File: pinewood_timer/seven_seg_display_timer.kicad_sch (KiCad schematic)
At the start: 40 parts, among them M1 N-MOSFET, M10 N-MOSFET, M11 N-MOSFET, M12 N-MOSFET, M13 N-MOSFET, M14 N-MOSFET, M15 N-MOSFET, M16 N-MOSFET, M2 N-MOSFET, M3 N-MOSFET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

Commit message: did some more work on the time displays
pb and pa maybe or pc. pa might need to be adc if i cant just transistor/relay it or something
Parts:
- added R17, R18, R19, R20, R21, R22, R23, R24, R25, R26, R27, R28, R29, R30, R31, R32: 47Ω, symbol Device:R_Small_US
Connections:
- net +3.3V: now also U6.6 (E2), U7.6 (E2)
- net R3: now reaches R3.2
- net R3: now also U6.13 (~{Y2})
- net R26: now reaches R10.2
- net R26: now also U7.14 (~{Y1})
- net R31: now reaches R15.2
- net R31: now also U7.9 (~{Y6})
- net R25: now reaches R9.2
- net R25: now also U7.15 (~{Y0})
- net R28: now reaches R12.2
- net R28: now also U7.12 (~{Y3})
- net R29: now reaches R13.2
- net R29: now also U7.11 (~{Y4})
- net R6: now reaches R6.2
- net R6: now also U6.10 (~{Y5})
- net C6: now reaches U3.1
- net E: now reaches U3.11
- net E: now also U2.11, R24.2
- net D: now reaches U3.13
- net D: now also U2.13, R23.2
- net C: now reaches U3.14
- net C: now also U2.14, R22.2
- net B: now reaches U3.15
- net B: now also U2.15, R21.2
- net A: now reaches U3.16
- net A: now also U2.16, R20.2
- net C5: now reaches U3.2
- net F: now reaches U3.3
- net F: now also U2.3, R17.2
- net G: now reaches U3.5
- net G: now also U2.5, R18.2
- net C8: now reaches U3.6
- net H: now reaches U3.7
- net H: now also U2.7, R19.2
- net C7: now reaches U3.8
- net R1: now reaches R1.2
- net R1: now also U6.15 (~{Y0})
- net GND: now reaches U8.11 (GND)
- net GND: now also U6.4 (~{E0}), U6.5 (~{E1}), U6.8 (GND), U7.4 (~{E0}), U7.5 (~{E1}), U7.8 (GND), U9.11 (GND)
- net at U8.12 (*Y8): now also R24.1
- net at U8.13 (*Y7): now also R23.1
- net at U8.14 (*Y6): now also R22.1
- net at U8.15 (*Y5): now also R21.1
- net at U8.16 (*Y4): now also R20.1
- net at U8.17 (*Y3): now also R19.1
- net at U8.18 (*Y2): now also R18.1
- net at U8.19 (*Y1): now also R17.1
- net R30: now reaches U7.10 (~{Y5})
- net R30: now also R14.2
- net R27: now reaches U7.13 (~{Y2})
- net R27: now also R11.2
- net R32: now reaches U7.7 (~{Y7})
- net R32: now also R16.2
- net at U9.12 (*Y8): now also R32.1
- net at U9.13 (*Y7): now also R31.1
- net at U9.14 (*Y6): now also R30.1
- net at U9.15 (*Y5): now also R29.1
- net at U9.16 (*Y4): now also R28.1
- net at U9.17 (*Y3): now also R27.1
- net at U9.18 (*Y2): now also R26.1
- net at U9.19 (*Y1): now also R25.1
- net R7: now reaches R7.2
- net R7: now also U6.9 (~{Y6})
- net R8: now reaches R8.2
- net R8: now also U6.7 (~{Y7})
- net R4: now reaches R4.2
- net R4: now also U6.12 (~{Y3})
- net R5: now reaches R5.2
- net R5: now also U6.11 (~{Y4})
- net R2: now reaches U6.14 (~{Y1})
- net R2: now also R2.2
- net C2: now reaches U2.1
- net C1: now reaches U2.2
- net C4: now reaches U2.6
- net C3: now reaches U2.8
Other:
- note added: "NOTHING"
- note added: "PA"
- note added: "PB8-10"
- moved on the sheet: U8, U9

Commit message: worked on schematic more
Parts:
- R1: value 150Ω -> reveiver
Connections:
- net C10: now also U4.1
- net C11: now also U4.8
- net C12: now also U4.6
- net C13: now also U5.2
- net C14: now also U5.1
- net C15: now also U5.8
- net C16: now also U5.6
- net C2: now also R30.2, U4.14, U5.14
- net C9: now also U4.2
- net PB0: now also U8.7 (D6)
- net PB1: now also U8.5 (D4)
- net PB10: now also U6.3 (A2)
- net PB2: now also U8.8 (D7)
- net PB3: now also U8.2 (D1)
- net PB4: now also U8.3 (D2)
- net PB5: now also U8.9 (D8)
- net PB6: now also U8.6 (D5)
- net PB7: now also U8.4 (D3)
- net PB8: now also U6.1 (A0)
- net PB9: now also U6.2 (A1)
- net R1: no longer R1.2
- net F2: now reaches R25.2
- net F2: now also U4.3, U5.3
- net D2: now reaches R31.2
- net D2: now also U4.13, U5.13
- net G2: now reaches R26.2
- net G2: now also U4.5, U5.5
- net E2: now reaches R32.2
- net E2: now also U4.11, U5.11
- net B2: now reaches U4.15
- net B2: now also R29.2, U5.15
- net A2: now reaches U4.16
- net A2: now also R28.2, U5.16
- net H2: now reaches U4.7
- net H2: now also R27.2, U5.7
- net PC8: now reaches U7.1 (A0)
- net PC9: now reaches U7.2 (A1)
- net PC10: now reaches U7.3 (A2)
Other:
- note removed: "PA"
- title: (none) -> TIME_DISPLAYS

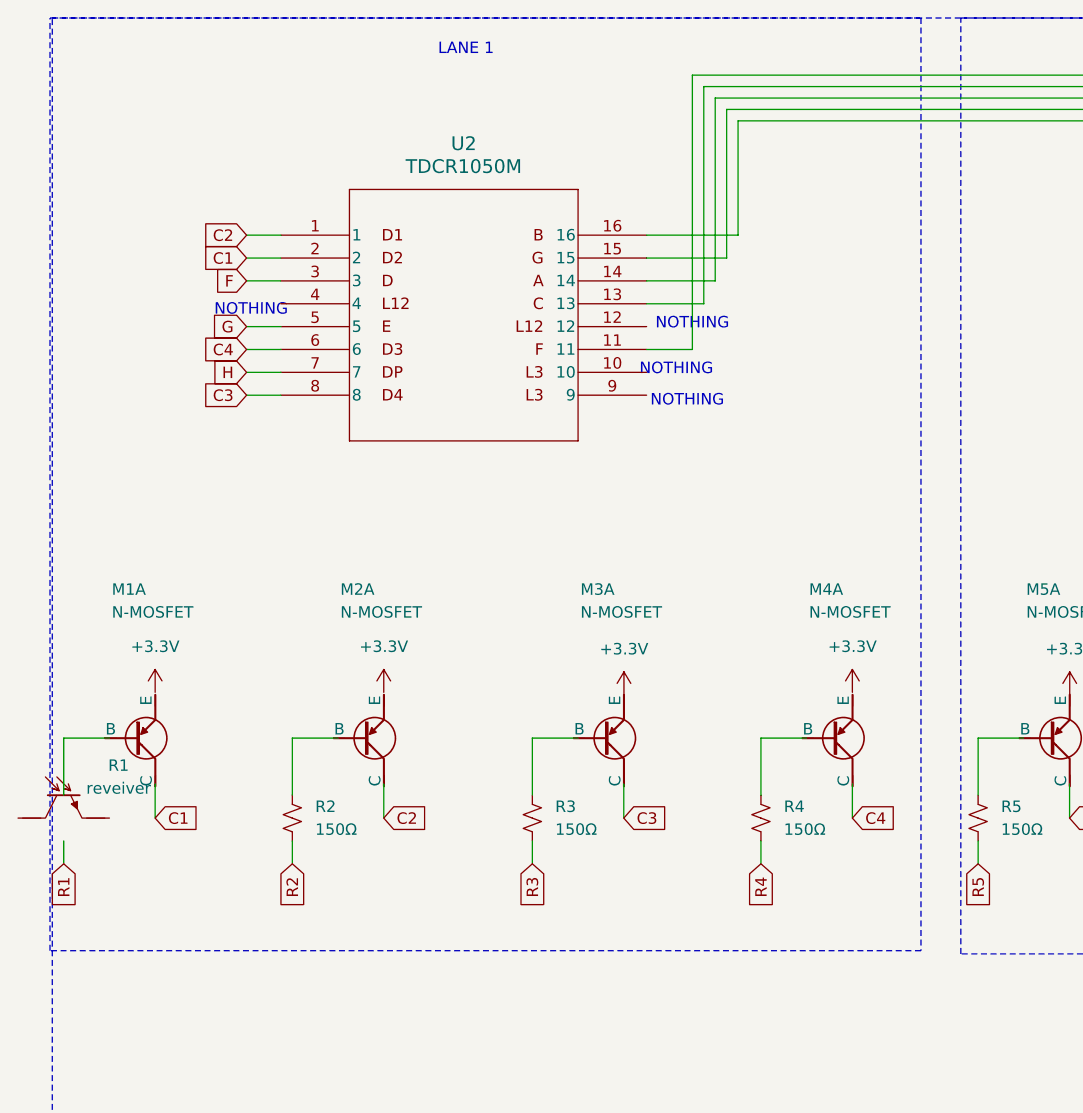
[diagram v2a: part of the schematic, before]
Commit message: edited schematic
added descriptions to sheets
chose sensor pins
added missing items to bom
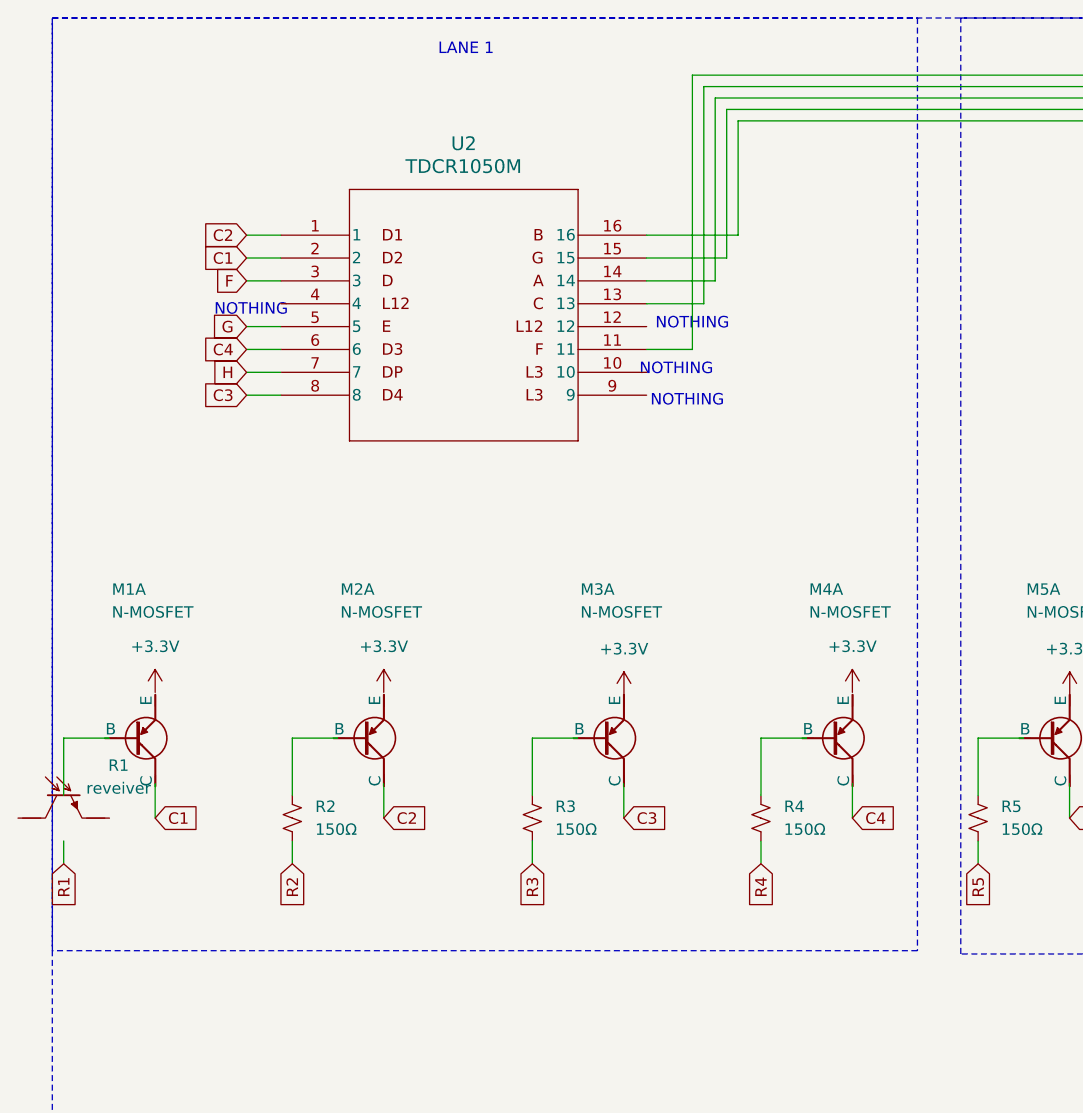
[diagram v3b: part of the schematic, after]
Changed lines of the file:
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@@
 	)
 	(rectangle
-		(start 13.716 13.9699)
-		(end 110.49 117.602)
+		(start 13.9808 13.9698)
+		(end 110.0986 117.6019)
 		(stroke
 			(width 0)

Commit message: added pins
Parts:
- added J2, J3: Conn_01x12_Pin, symbol Connector:Conn_01x12_Pin
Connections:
- net +3.3V: now also J2.1 (Pin_1)
- net GND: now also J3.1 (Pin_1)
- net PB0: now also J2.2 (Pin_2)
- net PB1: now also J2.3 (Pin_3)
- net PB10: now also J2.12 (Pin_12)
- net PB2: now also J2.4 (Pin_4)
- net PB3: now also J2.5 (Pin_5)
- net PB4: now also J2.6 (Pin_6)
- net PB5: now also J2.7 (Pin_7)
- net PB6: now also J2.8 (Pin_8)
- net PB7: now also J2.9 (Pin_9)
- net PB8: now also J2.10 (Pin_10)
- net PB9: now also J2.11 (Pin_11)
- net PC0: now also J3.2 (Pin_2)
- net PC1: now also J3.3 (Pin_3)
- net PC10: now also J3.12 (Pin_12)
- net PC2: now also J3.4 (Pin_4)
- net PC3: now also J3.5 (Pin_5)
- net PC4: now also J3.6 (Pin_6)
- net PC5: now also J3.7 (Pin_7)
- net PC6: now also J3.8 (Pin_8)
- net PC7: now also J3.9 (Pin_9)
- net PC8: now also J3.10 (Pin_10)
- net PC9: now also J3.11 (Pin_11)

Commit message: worked on the ir sensors and placement display
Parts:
- R1: value reveiver -> 150Ω
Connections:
- net R1: now also R1.2
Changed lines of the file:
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@@
-	)
-	(symbol
-		(lib_name "R_Small_US_1")
-		(lib_id "Device:R_Small_US")
-		(at 15.24 102.87 0)
-		(unit 1)
-		(exclude_from_sim no)
-		(in_bom yes)
-		(on_board yes)
-		(dnp no)
-		(property "Reference" "R1"
-			(at 21.336 97.028 0)
-			(effects
-				(font
-					(size 1.27 1.27)
-				)
-			)
-		)
-		(property "Value" "reveiver"
-			(at 21.336 99.568 0)
-			(effects
-				(font
-					(size 1.27 1.27)
-				)
-			)
-		)
-		(property "Footprint" ""
-			(at 15.24 102.87 0)
-			(effects
-				(font
-					(size 1.27 1.27)
-				)
-				(hide yes)
-			)
-		)
-		(property "Datasheet" "~"
-			(at 16.002 94.234 0)
-			(effects
-				(font
-					(size 1.27 1.27)
-				)
-				(hide yes)
-			)
-		)
-		(property "Description" "led receiver"
-			(at 6.35 93.98 0)
-			(effects
-				(font
-					(size 1.27 1.27)
-				)
-				(hide yes)
-			)
-		)
-		(pin "2"
-		)
-		(pin "1"
-		)
-		(instances
-			(project ""
-				(path "/8c59d8ce-9b8d-4f28-8062-629d479db88d/3afa3ac3-963c-4392-ab61-de1e7344ddd6"
-					(reference "R1")
-					(unit 1)
-				)
-				(path "/8c59d8ce-9b8d-4f28-8062-629d479db88d/9c18d310-d9ca-41af-922a-8b61f0cbe385"
-					(reference "R1")
-					(unit 1)
-				)
-			)
-		)
 	)
 	(symbol
@@
 					(unit 1)
 				)
+			)
+		)
+	)
+	(symbol
+		(lib_id "Device:R_Small_US")
+		(at 15.24 102.87 0)
+		(unit 1)
+		(exclude_from_sim no)
+		(in_bom yes)
+		(on_board yes)
+		(dnp no)
+		(property "Reference" "R1"
+			(at 17.78 101.5999 0)
+			(effects
+				(font
+					(size 1.27 1.27)
+				)
+				(justify left)
+			)
+		)
+		(property "Value" "150Ω"
+			(at 17.78 104.1399 0)
+			(effects
+				(font
+					(size 1.27 1.27)
+				)
+				(justify left)
+			)
+		)
+		(property "Footprint" ""
+			(at 15.24 102.87 0)
+			(effects
+				(font
+					(size 1.27 1.27)
+				)
+				(hide yes)
+			)
+		)
+		(property "Datasheet" "~"
+			(at 15.24 102.87 0)
+			(effects
+				(font
+					(size 1.27 1.27)
+				)
+				(hide yes)
+			)
+		)
+		(property "Description" "Resistor, small US symbol"
+			(at 15.24 102.87 0)
+			(effects
+				(font
+					(size 1.27 1.27)
+				)
+				(hide yes)
+			)
+		)
+		(pin "2"
+		)
+		(pin "1"
+		)
+		(instances
+			(project "pinewood_timer"
+				(path "/8c59d8ce-9b8d-4f28-8062-629d479db88d/3afa3ac3-963c-4392-ab61-de1e7344ddd6"
+					(reference "R1")
+					(unit 1)
+				)

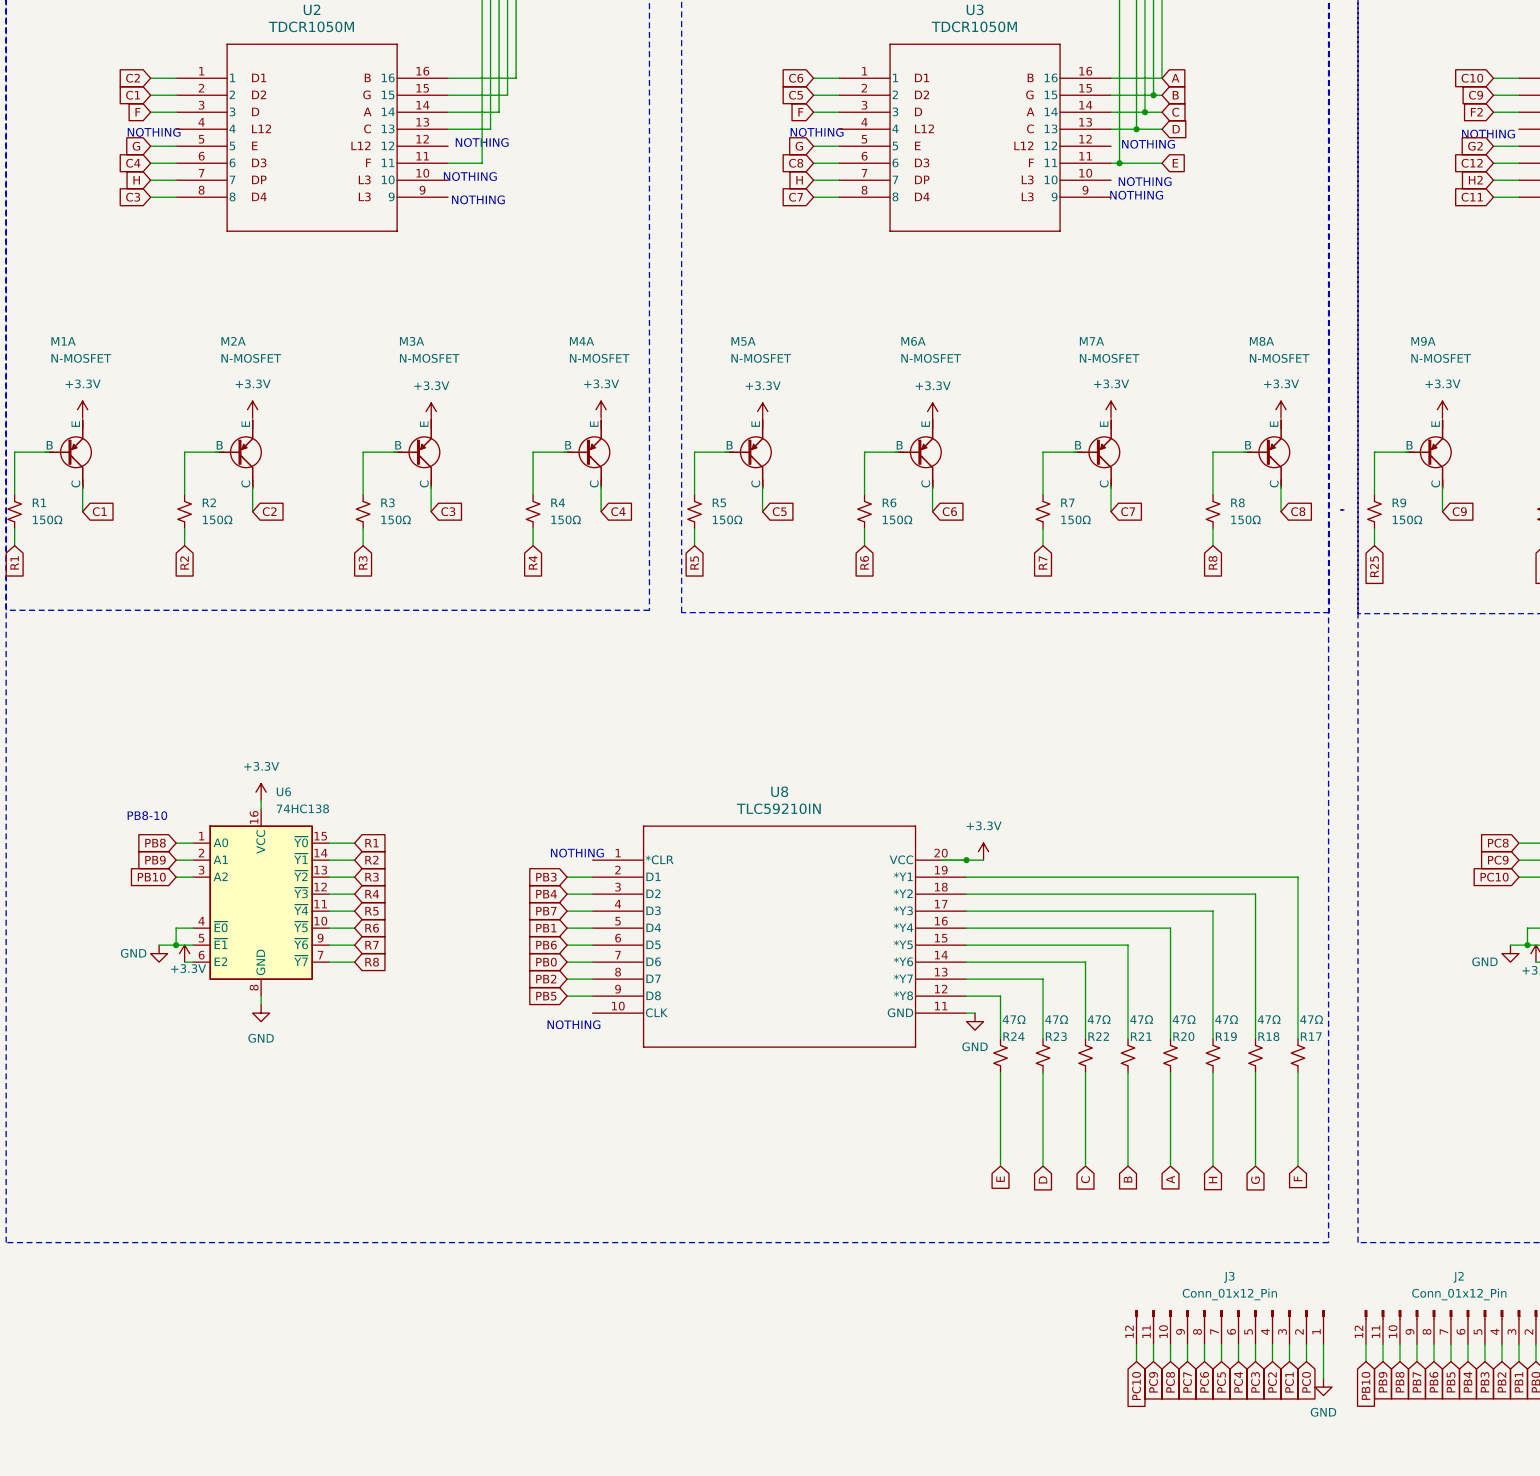
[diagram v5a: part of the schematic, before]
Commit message: edited placement timer schematic since i can never make up my mind
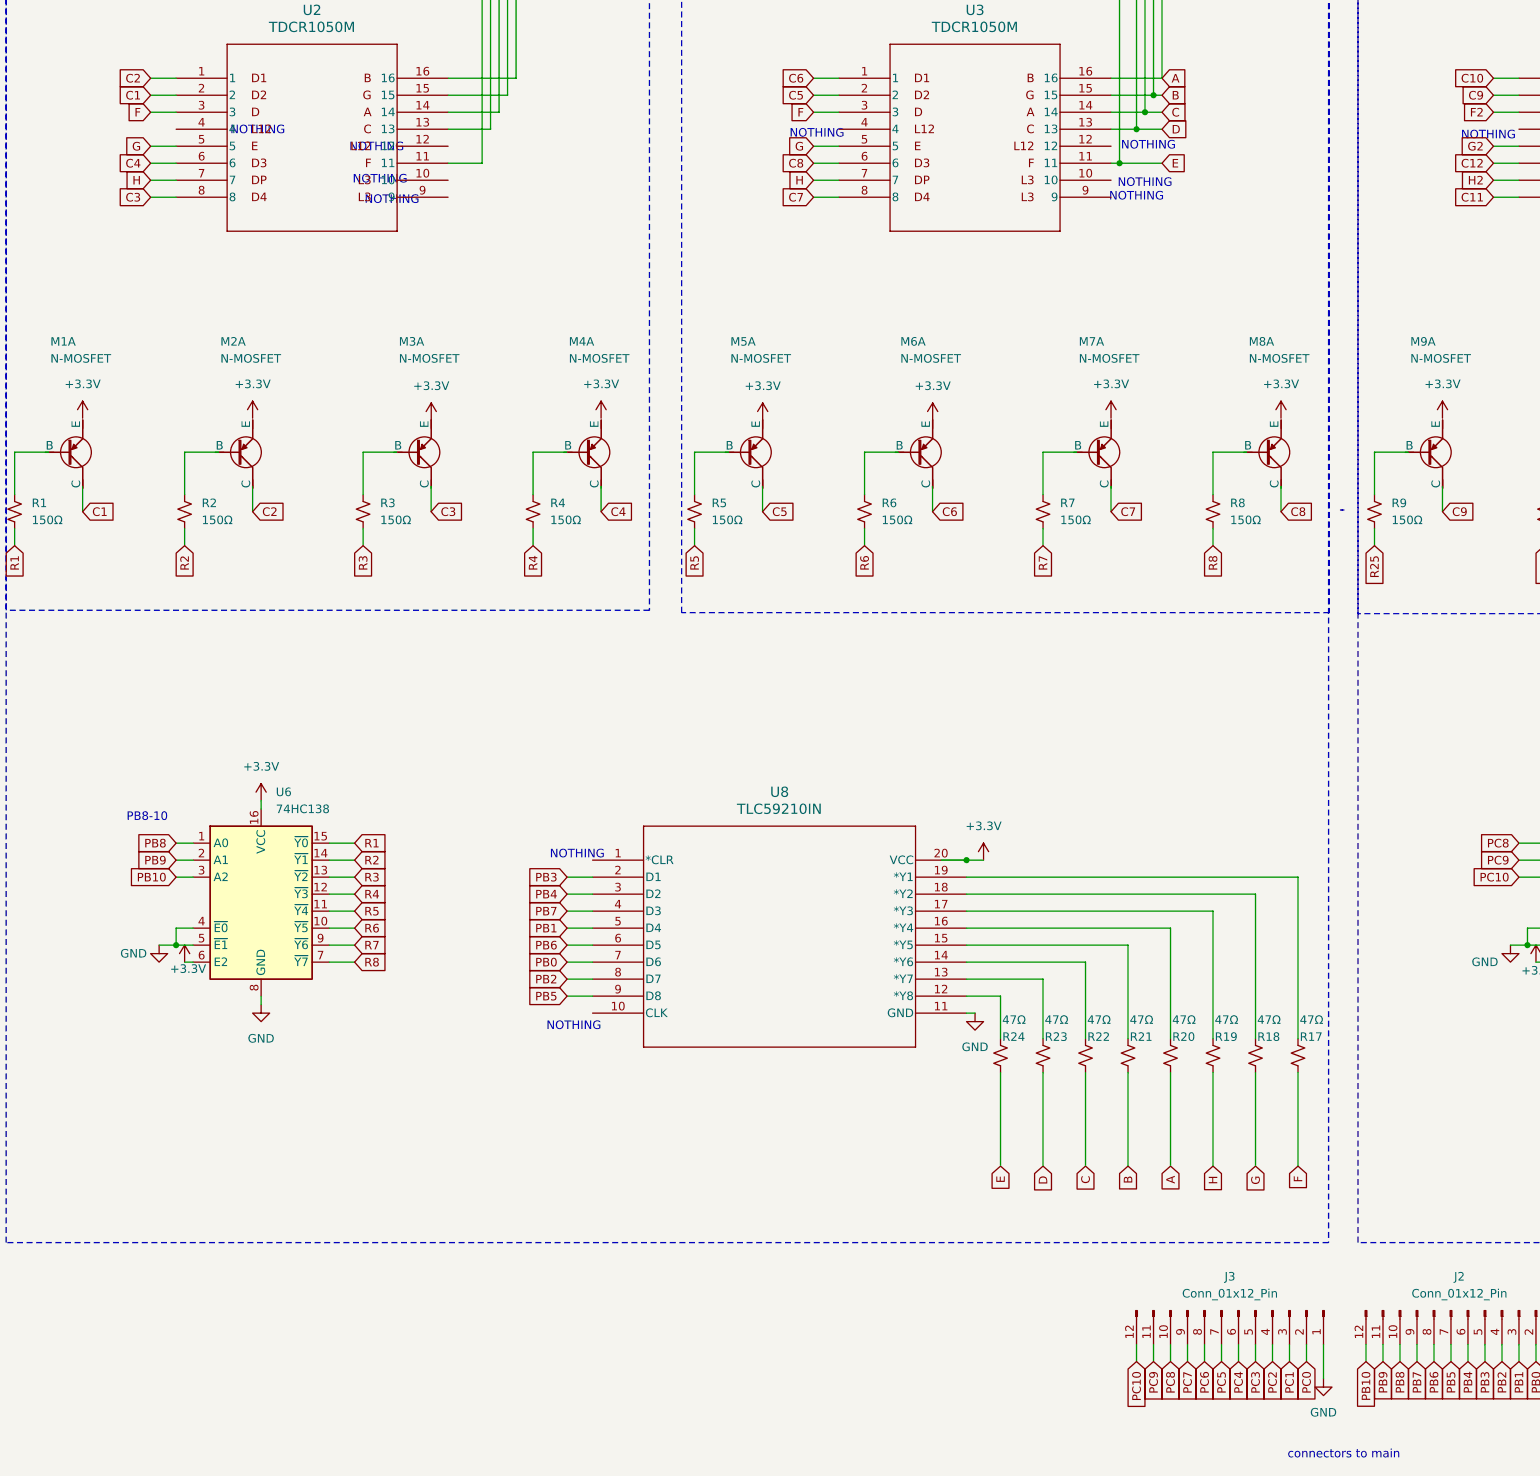
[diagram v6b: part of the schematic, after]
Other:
- note added: "connectors to main"
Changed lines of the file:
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@@
 	(text "NOTHING"
 		(exclude_from_sim no)
-		(at 84.5272 56.57 0)
+		(at 71.628 56.388 0)
 		(effects
 			(font
@@
 	(text "NOTHING"
 		(exclude_from_sim no)
-		(at 83.312 53.086 0)
+		(at 69.85 53.34 0)
 		(effects
 			(font
@@
 	(text "NOTHING"
 		(exclude_from_sim no)
-		(at 36.068 46.482 0)
+		(at 51.562 45.974 0)
 		(effects
 			(font
@@
 	(text "NOTHING"
 		(exclude_from_sim no)
-		(at 85.09 48.006 0)
+		(at 69.342 48.514 0)
 		(effects
 			(font
@@
 		(effects
 			(font
+				(size 1.27 1.27)
+			)
+		)
+	)
+	(text "connectors to main"
+		(exclude_from_sim no)
+		(at 213.868 243.84 0)
+		(effects
+			(font
